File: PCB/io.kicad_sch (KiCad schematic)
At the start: 14 parts, among them SW3 Hand Switch, U9 OLED_Waveshare

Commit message: begin BOM
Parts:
- C? (x3): footprint (none) -> Capacitor_SMD:C_0603_1608Metric; MPN (none) -> CGA3E2X7R1H104M080AA; Manufacturer (none) -> TDK
- C? (x2): footprint (none) -> Capacitor_SMD:C_0603_1608Metric; MPN (none) -> GCM188R71H103KA37J; Manufacturer (none) -> Murata
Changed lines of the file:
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@@
     (effects (font (size 1.27 1.27)) (justify left bottom))
   )
-  (label "OLED.MOSI" (at 177.8 58.42 180)
+  (label "OLED.MOSI" (at 177.8 58.42 180) (fields_autoplaced)
     (effects (font (size 1.27 1.27)) (justify right bottom))
   )
@@
     (effects (font (size 1.27 1.27)) (justify left bottom))
   )
-  (label "OLED.SCK" (at 177.8 60.96 180)
+  (label "OLED.SCK" (at 177.8 60.96 180) (fields_autoplaced)
     (effects (font (size 1.27 1.27)) (justify right bottom))
   )
@@
     (effects (font (size 1.27 1.27)) (justify right bottom))
   )
-  (label "OLED.~{CS}" (at 177.8 63.5 180)
+  (label "OLED.~{CS}" (at 177.8 63.5 180) (fields_autoplaced)
     (effects (font (size 1.27 1.27)) (justify right bottom))
   )
@@
     )
     (property "Datasheet" "~" (at 87.63 58.166 0)
+      (effects (font (size 1.27 1.27)) hide)
+    )
+    (property "MPN" "" (at 87.63 64.77 0)
+      (effects (font (size 1.27 1.27)) hide)
+    )
+    (property "Manufacturer" "" (at 87.63 64.77 0)
       (effects (font (size 1.27 1.27)) hide)
     )
@@
       (effects (font (size 1.27 1.27)))
     )
-    (property "Footprint" "" (at 69.85 63.1952 0)
+    (property "Footprint" "Capacitor_SMD:C_0603_1608Metric" (at 69.85 63.1952 0)
       (effects (font (size 1.27 1.27)) hide)
     )
@@
       (effects (font (size 1.27 1.27)) hide)
     )
+    (property "MPN" "CGA3E2X7R1H104M080AA " (at 66.04 62.23 0)
+      (effects (font (size 1.27 1.27)) hide)
+    )
+    (property "Manufacturer" "TDK" (at 66.04 62.23 0)
+      (effects (font (size 1.27 1.27)) hide)
+    )
     (pin "1")
     (pin "2")
@@
       (effects (font (size 1.27 1.27)))
     )
-    (property "Footprint" "" (at 62.23 66.3448 0)
+    (property "Footprint" "Capacitor_SMD:C_0603_1608Metric" (at 62.23 66.3448 0)
       (effects (font (size 1.27 1.27)) hide)
     )
@@
       (effects (font (size 1.27 1.27)) hide)
     )
+    (property "MPN" "CGA3E2X7R1H104M080AA " (at 66.04 67.31 0)
+      (effects (font (size 1.27 1.27)) hide)
+    )
+    (property "Manufacturer" "TDK" (at 66.04 67.31 0)
+      (effects (font (size 1.27 1.27)) hide)
+    )
     (pin "1")
     (pin "2")
@@
     )
     (property "Datasheet" "~" (at 76.2 142.24 0)
+      (effects (font (size 1.27 1.27)) hide)
+    )
+    (property "MPN" "" (at 76.2 142.24 0)
+      (effects (font (size 1.27 1.27)) hide)
+    )
+    (property "Manufacturer" "" (at 76.2 142.24 0)
       (effects (font (size 1.27 1.27)) hide)
     )
@@
       (effects (font (size 1.27 1.27)))
     )
-    (property "Footprint" "" (at 186.9948 139.7 0)
+    (property "Footprint" "Capacitor_SMD:C_0603_1608Metric" (at 186.9948 139.7 0)
       (effects (font (size 1.27 1.27)) hide)
     )
@@
       (effects (font (size 1.27 1.27)) hide)
     )
+    (property "MPN" "GCM188R71H103KA37J" (at 187.96 135.89 0)
+      (effects (font (size 1.27 1.27)) hide)
+    )
+    (property "Manufacturer" "Murata" (at 187.96 135.89 0)
+      (effects (font (size 1.27 1.27)) hide)
+    )
     (pin "1")
     (pin "2")
@@
       (effects (font (size 1.27 1.27)) hide)
     )
+    (property "MPN" "" (at 172.72 124.46 0)
+      (effects (font (size 1.27 1.27)) hide)
+    )
+    (property "Manufacturer" "" (at 172.72 124.46 0)
+      (effects (font (size 1.27 1.27)) hide)
+    )
     (pin "1")
     (pin "2")
@@
       (effects (font (size 1.27 1.27)) hide)
     )
+    (property "MPN" "" (at 69.85 57.15 0)
+      (effects (font (size 1.27 1.27)) hide)
+    )
+    (property "Manufacturer" "" (at 69.85 57.15 0)
+      (effects (font (size 1.27 1.27)) hide)
+    )
     (pin "1")
     (pin "2")
@@
       (effects (font (size 1.27 1.27)))
     )
-    (property "Footprint" "" (at 104.4448 68.58 0)
+    (property "Footprint" "Capacitor_SMD:C_0603_1608Metric" (at 104.4448 68.58 0)
       (effects (font (size 1.27 1.27)) hide)
     )
@@
       (effects (font (size 1.27 1.27)) hide)
     )
+    (property "MPN" "CGA3E2X7R1H104M080AA " (at 105.41 64.77 0)
+      (effects (font (size 1.27 1.27)) hide)
+    )
+    (property "Manufacturer" "TDK" (at 105.41 64.77 0)
+      (effects (font (size 1.27 1.27)) hide)
+    )
     (pin "1")
     (pin "2")
@@
     )
     (property "Datasheet" "~" (at 85.09 129.54 0)
+      (effects (font (size 1.27 1.27)) hide)
+    )
+    (property "MPN" "" (at 85.09 129.54 0)
+      (effects (font (size 1.27 1.27)) hide)
+    )
+    (property "Manufacturer" "" (at 85.09 129.54 0)
       (effects (font (size 1.27 1.27)) hide)
     )
@@
     )
     (property "Datasheet" "" (at 186.69 53.34 0)
+      (effects (font (size 1.27 1.27)) hide)
+    )
+    (property "MPN" "" (at 193.04 63.5 0)
+      (effects (font (size 1.27 1.27)) hide)
+    )
+    (property "Manufacturer" "" (at 193.04 63.5 0)
       (effects (font (size 1.27 1.27)) hide)
     )
@@
       (effects (font (size 1.27 1.27)) hide)
     )
+    (property "MPN" "" (at 101.6 54.61 0)
+      (effects (font (size 1.27 1.27)) hide)
+    )
+    (property "Manufacturer" "" (at 101.6 54.61 0)
+      (effects (font (size 1.27 1.27)) hide)
+    )
     (pin "1")
     (pin "2")
@@
       (effects (font (size 1.27 1.27)))
     )
-    (property "Footprint" "" (at 91.7448 144.78 0)
+    (property "Footprint" "Capacitor_SMD:C_0603_1608Metric" (at 91.7448 144.78 0)
       (effects (font (size 1.27 1.27)) hide)
     )
@@
       (effects (font (size 1.27 1.27)) hide)
     )
+    (property "MPN" "GCM188R71H103KA37J" (at 92.71 140.97 0)
+      (effects (font (size 1.27 1.27)) hide)
+    )
+    (property "Manufacturer" "Murata" (at 92.71 140.97 0)
+      (effects (font (size 1.27 1.27)) hide)
+    )
     (pin "1")
     (pin "2")
@@
       (effects (font (size 1.27 1.27)) hide)
     )
+    (property "MPN" "" (at 69.85 72.39 0)
+      (effects (font (size 1.27 1.27)) hide)
+    )
+    (property "Manufacturer" "" (at 69.85 72.39 0)
+      (effects (font (size 1.27 1.27)) hide)
+    )
     (pin "1")
     (pin "2")
@@
       (effects (font (size 1.27 1.27)) hide)
     )
+    (property "MPN" "" (at 172.72 135.89 0)
+      (effects (font (size 1.27 1.27)) hide)
+    )
+    (property "Manufacturer" "" (at 172.72 135.89 0)
+      (effects (font (size 1.27 1.27)) hide)
+    )

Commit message: Resistors ok in BOM
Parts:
- R? (x5): footprint (none) -> Resistor_SMD:R_0603_1608Metric; MPN (none) -> ERJ-3EKF1002V; Manufacturer (none) -> Panasonic
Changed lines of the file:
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@@
       (effects (font (size 1.27 1.27)) (justify right))
     )
-    (property "Footprint" "" (at 174.498 124.46 90)
+    (property "Footprint" "Resistor_SMD:R_0603_1608Metric" (at 174.498 124.46 90)
       (effects (font (size 1.27 1.27)) hide)
     )
@@
       (effects (font (size 1.27 1.27)) hide)
     )
-    (property "MPN" "" (at 172.72 124.46 0)
-      (effects (font (size 1.27 1.27)) hide)
-    )
-    (property "Manufacturer" "" (at 172.72 124.46 0)
+    (property "MPN" "ERJ-3EKF1002V" (at 172.72 124.46 0)
+      (effects (font (size 1.27 1.27)) hide)
+    )
+    (property "Manufacturer" "Panasonic" (at 172.72 124.46 0)
       (effects (font (size 1.27 1.27)) hide)
     )
@@
       (effects (font (size 1.27 1.27)) (justify right))
     )
-    (property "Footprint" "" (at 71.628 57.15 90)
+    (property "Footprint" "Resistor_SMD:R_0603_1608Metric" (at 71.628 57.15 90)
       (effects (font (size 1.27 1.27)) hide)
     )
@@
       (effects (font (size 1.27 1.27)) hide)
     )
-    (property "MPN" "" (at 69.85 57.15 0)
-      (effects (font (size 1.27 1.27)) hide)
-    )
-    (property "Manufacturer" "" (at 69.85 57.15 0)
+    (property "MPN" "ERJ-3EKF1002V" (at 69.85 57.15 0)
+      (effects (font (size 1.27 1.27)) hide)
+    )
+    (property "Manufacturer" "Panasonic" (at 69.85 57.15 0)
       (effects (font (size 1.27 1.27)) hide)
     )
@@
       (effects (font (size 1.27 1.27)) (justify right))
     )
-    (property "Footprint" "" (at 86.868 129.54 90)
+    (property "Footprint" "Resistor_SMD:R_0603_1608Metric" (at 86.868 129.54 90)
       (effects (font (size 1.27 1.27)) hide)
     )
@@
       (effects (font (size 1.27 1.27)) hide)
     )
-    (property "MPN" "" (at 85.09 129.54 0)
-      (effects (font (size 1.27 1.27)) hide)
-    )
-    (property "Manufacturer" "" (at 85.09 129.54 0)
+    (property "MPN" "ERJ-3EKF1002V" (at 85.09 129.54 0)
+      (effects (font (size 1.27 1.27)) hide)
+    )
+    (property "Manufacturer" "Panasonic" (at 85.09 129.54 0)
       (effects (font (size 1.27 1.27)) hide)
     )
@@
       (effects (font (size 1.27 1.27)) (justify right))
     )
-    (property "Footprint" "" (at 103.378 54.61 90)
+    (property "Footprint" "Resistor_SMD:R_0603_1608Metric" (at 103.378 54.61 90)
       (effects (font (size 1.27 1.27)) hide)
     )
@@
       (effects (font (size 1.27 1.27)) hide)
     )
-    (property "MPN" "" (at 101.6 54.61 0)
-      (effects (font (size 1.27 1.27)) hide)
-    )
-    (property "Manufacturer" "" (at 101.6 54.61 0)
+    (property "MPN" "ERJ-3EKF1002V" (at 101.6 54.61 0)
+      (effects (font (size 1.27 1.27)) hide)
+    )
+    (property "Manufacturer" "Panasonic" (at 101.6 54.61 0)
       (effects (font (size 1.27 1.27)) hide)
     )
@@
       (effects (font (size 1.27 1.27)) (justify right))
     )
-    (property "Footprint" "" (at 71.628 72.39 90)
+    (property "Footprint" "Resistor_SMD:R_0603_1608Metric" (at 71.628 72.39 90)
       (effects (font (size 1.27 1.27)) hide)
     )
@@
       (effects (font (size 1.27 1.27)) hide)
     )
-    (property "MPN" "" (at 69.85 72.39 0)
-      (effects (font (size 1.27 1.27)) hide)
-    )
-    (property "Manufacturer" "" (at 69.85 72.39 0)
-      (effects (font (size 1.27 1.27)) hide)
-    )
+    (property "MPN" "ERJ-3EKF1002V" (at 69.85 72.39 0)
+      (effects (font (size 1.27 1.27)) hide)
+    )
+    (property "Manufacturer" "Panasonic" (at 69.85 72.39 0)
+      (effects (font (size 1.27 1.27)) hide)
+    )

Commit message: bom almost finished
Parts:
- J?: MPN (none) -> MJ-63022A; Manufacturer (none) -> CUI Devices
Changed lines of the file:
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@@
       (effects (font (size 1.27 1.27)) hide)
     )
-    (property "MPN" "" (at 76.2 142.24 0)
+    (property "MPN" "MJ-63022A" (at 76.2 142.24 0)
       (effects (font (size 1.27 1.27)) hide)
     )
-    (property "Manufacturer" "" (at 76.2 142.24 0)
+    (property "Manufacturer" "CUI Devices" (at 76.2 142.24 0)
       (effects (font (size 1.27 1.27)) hide)
     )

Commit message: continue bom
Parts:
- J?: footprint (none) -> TattooSupplyFootprints:MJ63022A
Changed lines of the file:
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@@
       (effects (font (size 1.27 1.27)) (justify right))
     )
-    (property "Footprint" "" (at 76.2 142.24 0)
+    (property "Footprint" "TattooSupplyFootprints:MJ63022A" (at 76.2 142.24 0)
       (effects (font (size 1.27 1.27)) hide)
     )

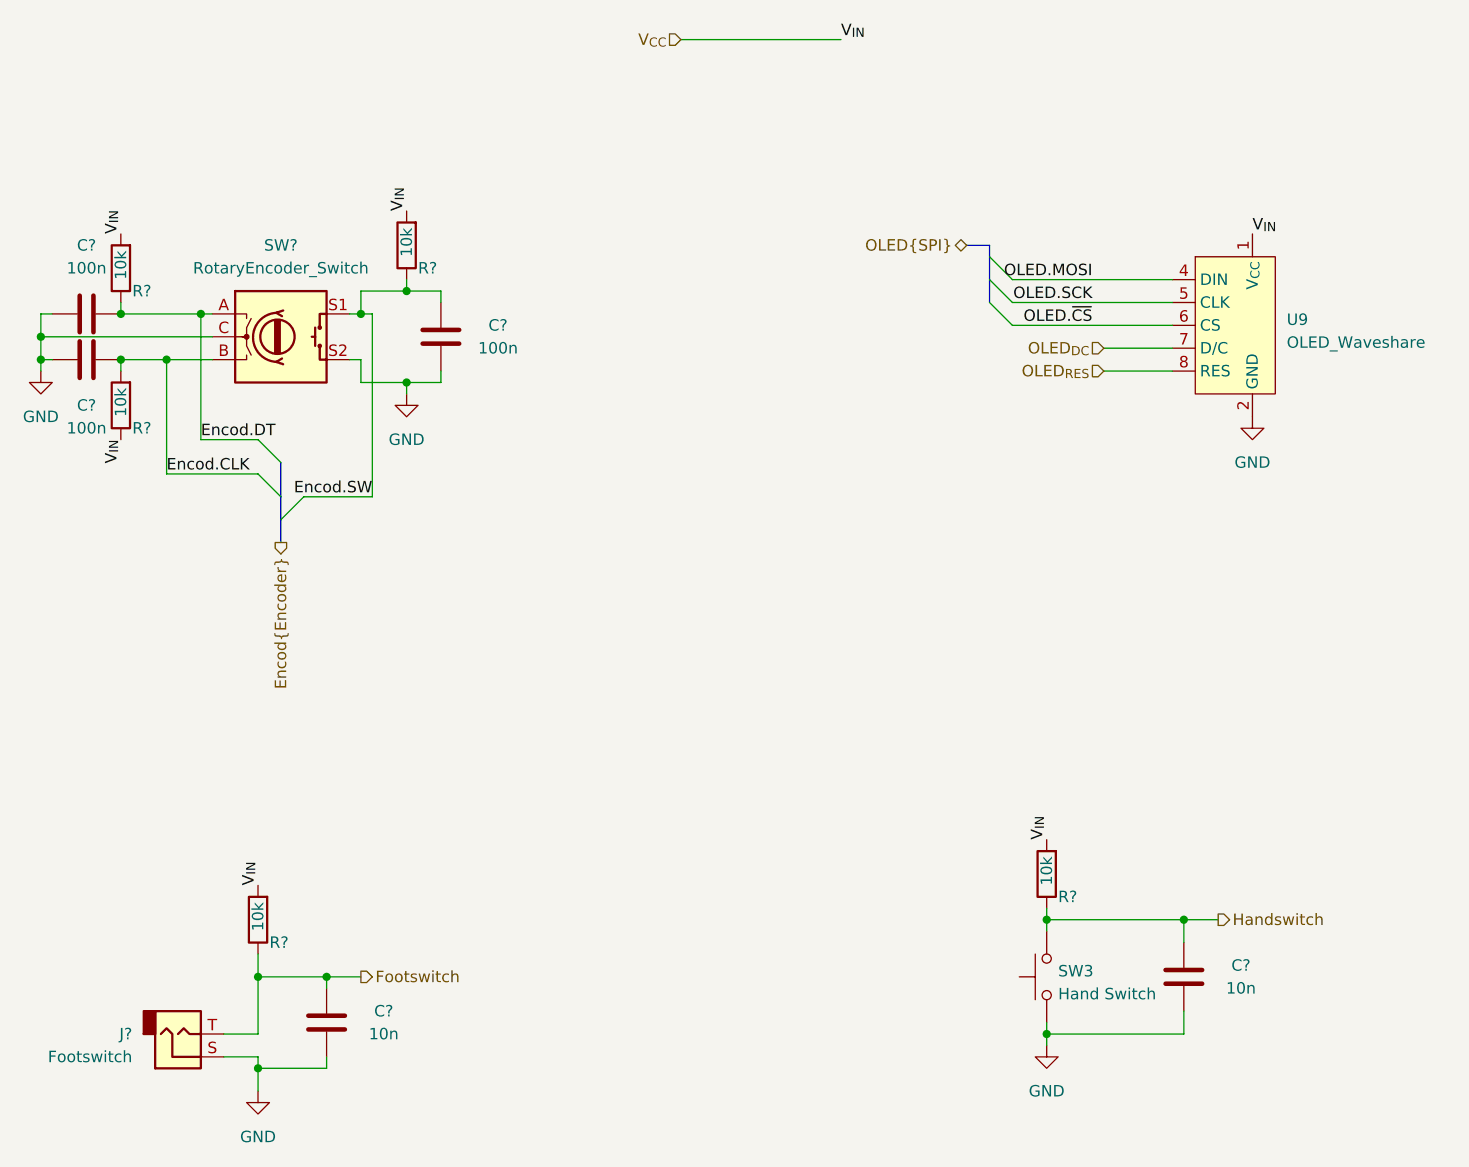
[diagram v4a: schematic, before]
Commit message: schematic done and bom ok
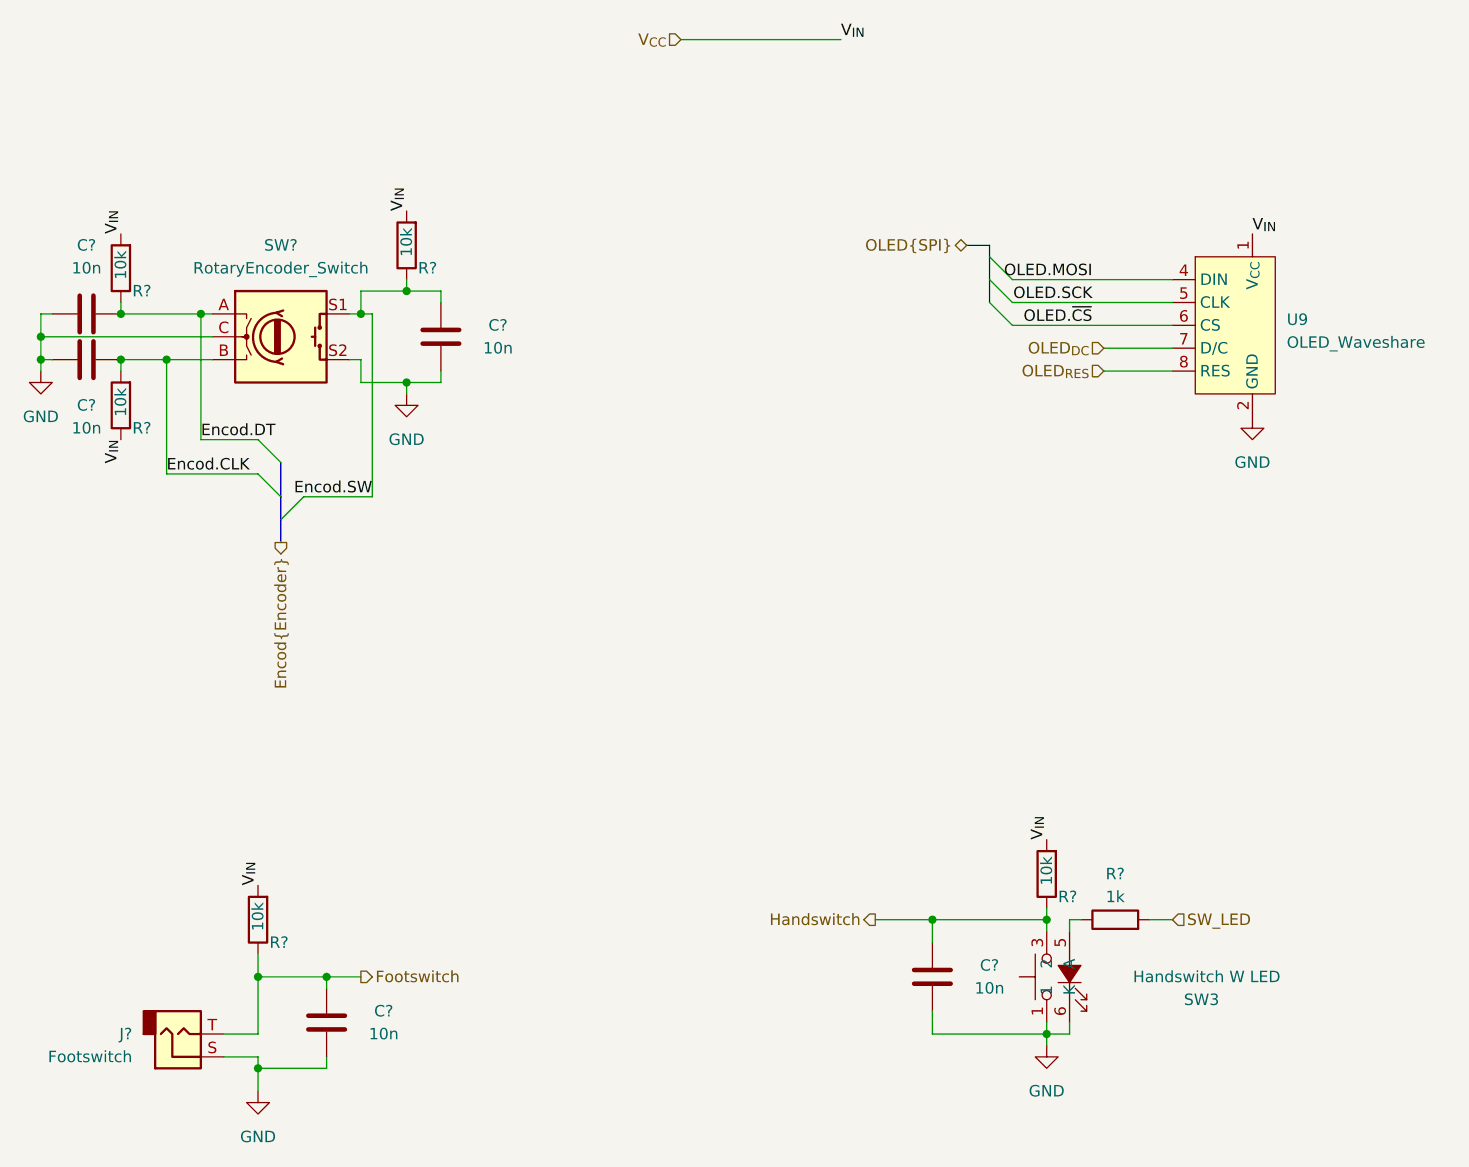
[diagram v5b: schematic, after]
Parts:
- removed SW3: Hand Switch, symbol Switch:SW_Push
- added R?: 1k, Resistor_SMD:R_0603_1608Metric, symbol Device:R
- added SW3: Handswitch W LED, TattooSupplyFootprints:D6RLxx, symbol TattooSupplyLib:PushButton_W_LED
- C? (x3): value 100n -> 10n; MPN CGA3E2X7R1H104M080AA -> GCM188R71H103KA37J; Manufacturer TDK -> Murata
- SW?: footprint (none) -> Rotary_Encoder:RotaryEncoder_Alps_EC11E-Switch_Vertical_H20mm; MPN (none) -> PEC11R-4220F-S0024; Manufacturer (none) -> Bourns
- U9: MPN (none) -> Waveshare; Manufacturer (none) -> 10451
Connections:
- net GND: now also SW3.1, SW3.2 (1), SW3.6 (K)
- net Handswitch: now also SW3.3 (2), SW3.4 (2)
- new net: R?.1, SW3.5 (A)
- new net SW_LED: R?.2
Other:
- moved on the sheet: C?
